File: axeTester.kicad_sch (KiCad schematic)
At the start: 43 parts

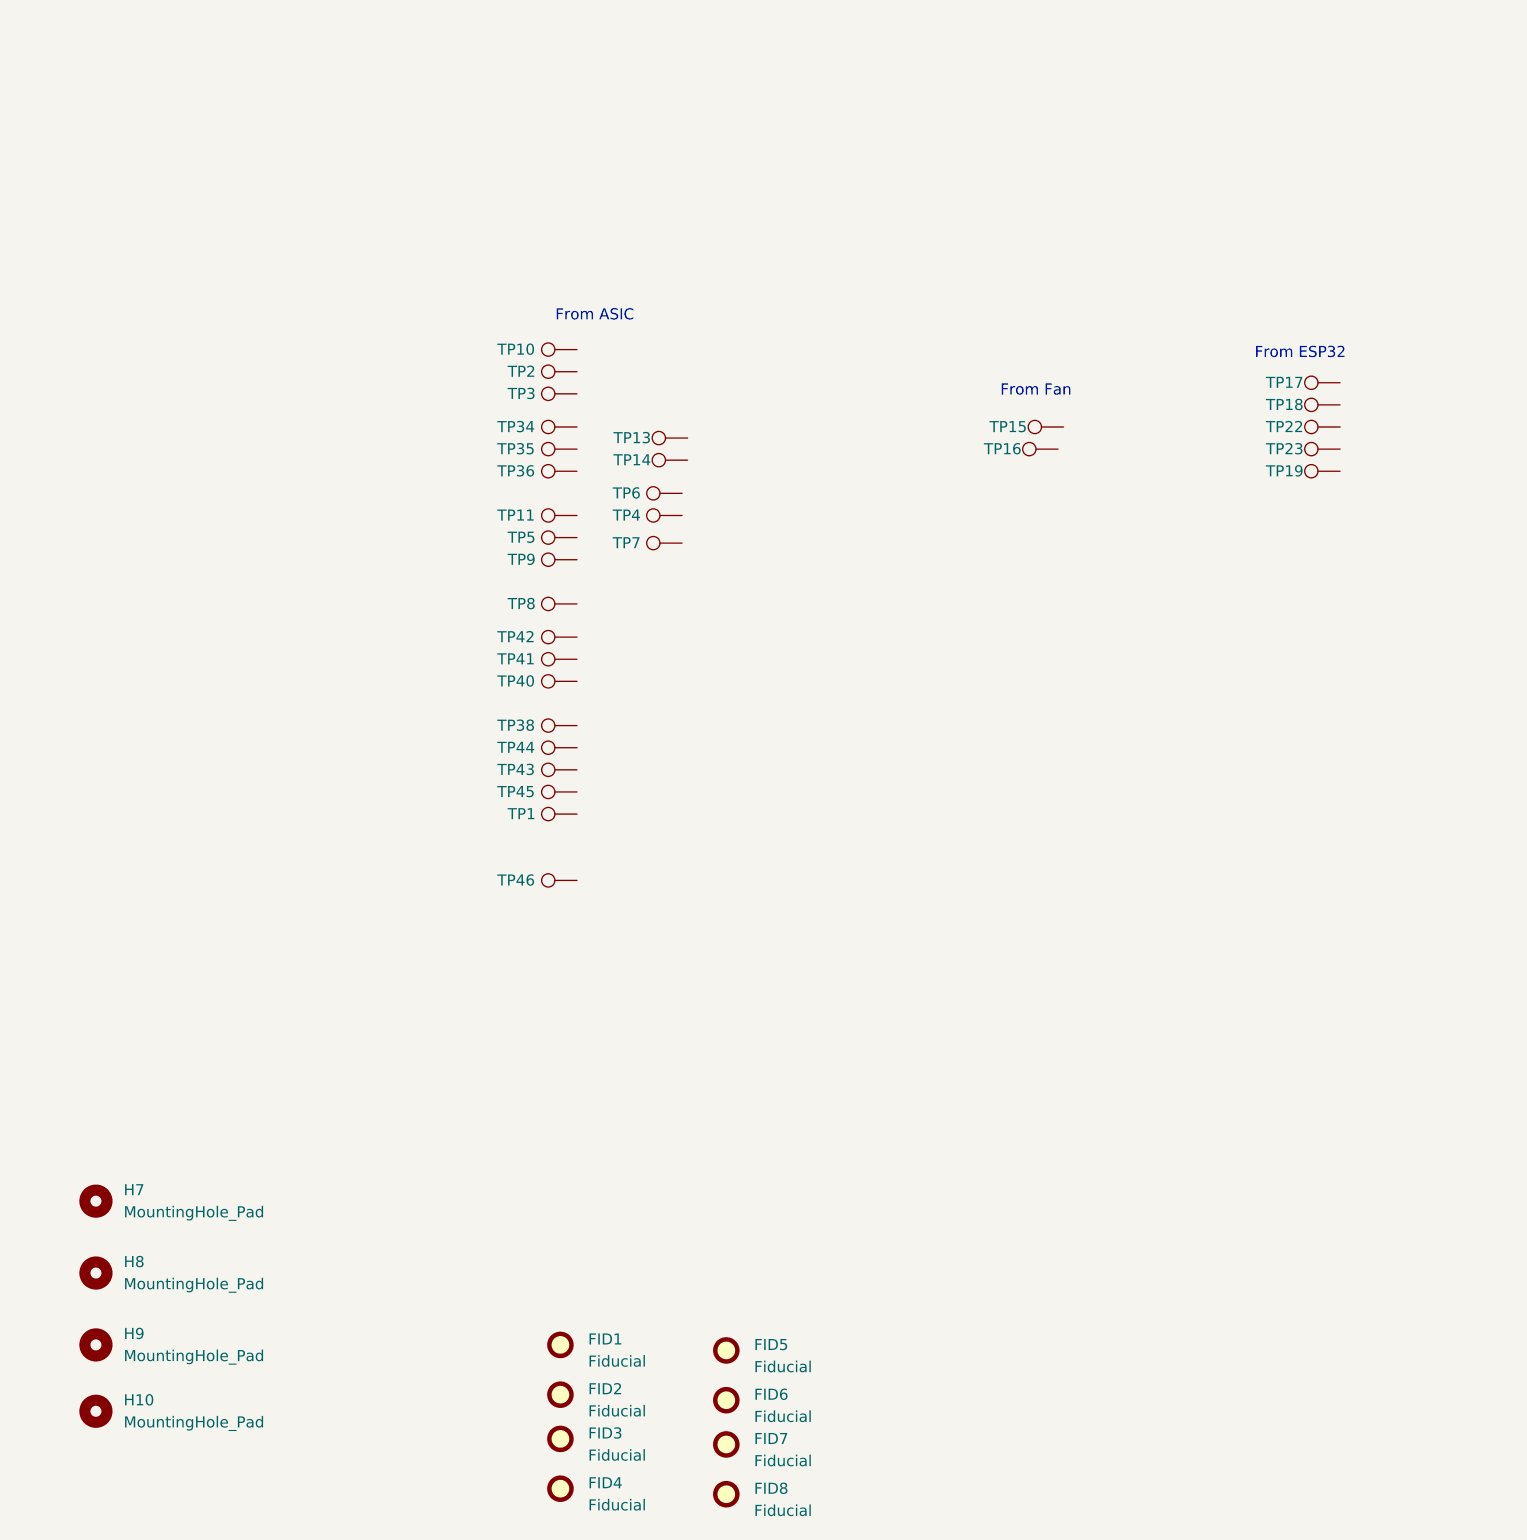
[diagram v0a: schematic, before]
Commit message: switched to more common THT pogo pins. wired up connectors
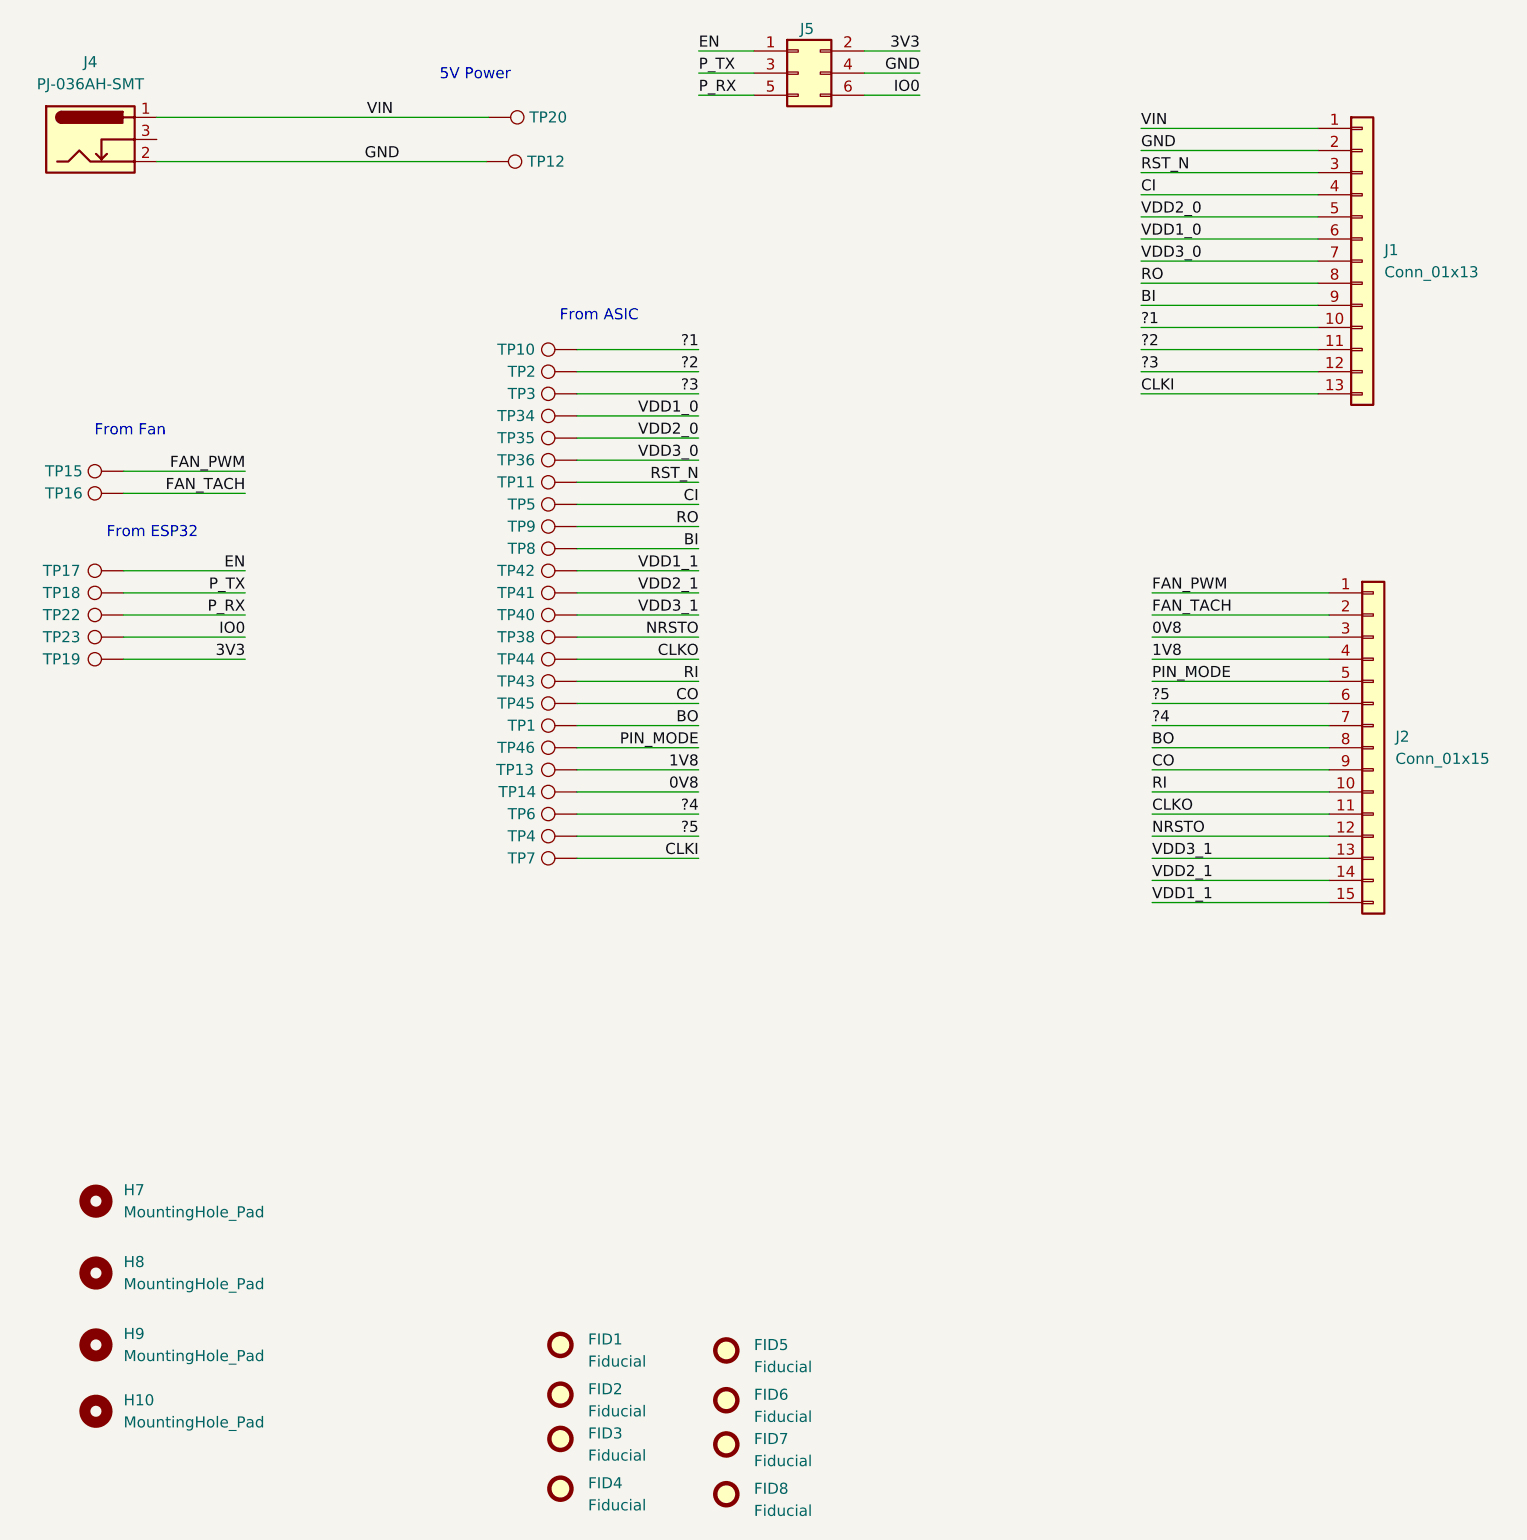
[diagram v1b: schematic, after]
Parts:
- added J1: Conn_01x13, Connector_PinHeader_2.54mm:PinHeader_1x13_P2.54mm_Horizontal, symbol Connector_Generic:Conn_01x13
- added J2: Conn_01x15, Connector_PinHeader_2.54mm:PinHeader_1x15_P2.54mm_Horizontal, symbol Connector_Generic:Conn_01x15
- added J4: PJ-036AH-SMT, Connector_BarrelJack:BarrelJack_CUI_PJ-036AH-SMT_Horizontal, symbol Connector:Barrel_Jack_Switch
- added J5: Conn_02x03_Counter_Clockwise, Connector_PinHeader_2.54mm:PinHeader_2x03_P2.54mm_Vertical, symbol Connector_Generic:Conn_02x03_Odd_Even
- added TP12, TP20: P75-E2, axeTester:pogopin-P75-E2-1.3, symbol Connector:TestPoint
- TP1, TP10, TP11, TP13, TP14, TP15, TP16, TP17, TP18, TP19, TP2, TP22, TP23, TP3, TP34, TP35, TP36, TP38, TP4, TP40, TP41, TP42, TP43, TP44, TP45, TP46, TP5, TP6, TP7, TP8, TP9: value TestPoint -> P50-E2; footprint TestPoint:TestPoint_Pad_D1.5mm -> axeTester:pogopin-P50-E2-0.68
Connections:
- net 1V8: now reaches TP13.1
- net 1V8: now also J2.4 (Pin_4)
- net P_TX: now reaches TP18.1
- net P_TX: now also J5.3 (Pin_3)
- net 3V3: now reaches TP19.1
- net 3V3: now also J5.2 (Pin_2)
- net EN: now reaches TP17.1
- net EN: now also J5.1 (Pin_1)
- net RI: now reaches TP43.1
- net RI: now also J2.10 (Pin_10)
- net CI: now reaches TP5.1
- net CI: now also J1.4 (Pin_4)
- net VDD2_1: now reaches TP41.1
- net VDD2_1: now also J2.14 (Pin_14)
- net BI: now reaches TP8.1
- net BI: now also J1.9 (Pin_9)
- net ?4: now reaches TP6.1
- net ?4: now also J2.7 (Pin_7)
- net VDD1_1: now reaches TP42.1
- net VDD1_1: now also J2.15 (Pin_15)
- net ?5: now reaches TP4.1
- net ?5: now also J2.6 (Pin_6)
- net PIN_MODE: now reaches TP46.1
- net PIN_MODE: now also J2.5 (Pin_5)
- net NRSTO: now reaches TP38.1
- net NRSTO: now also J2.12 (Pin_12)
- net VDD3_1: now reaches TP40.1
- net VDD3_1: now also J2.13 (Pin_13)
- net VDD1_0: now reaches TP34.1
- net VDD1_0: now also J1.6 (Pin_6)
- net FAN_TACH: now reaches TP16.1
- net FAN_TACH: now also J2.2 (Pin_2)
- net CO: now reaches TP45.1
- net CO: now also J2.9 (Pin_9)
- net ?3: now reaches TP3.1
- net ?3: now also J1.12 (Pin_12)
- net 0V8: now reaches TP14.1
- net 0V8: now also J2.3 (Pin_3)
- net FAN_PWM: now reaches TP15.1
- net FAN_PWM: now also J2.1 (Pin_1)
- net P_RX: now reaches TP22.1
- net P_RX: now also J5.5 (Pin_5)
- net RST_N: now reaches TP11.1
- net RST_N: now also J1.3 (Pin_3)
- net ?1: now reaches TP10.1
- net ?1: now also J1.10 (Pin_10)
- net VDD3_0: now reaches TP36.1
- net VDD3_0: now also J1.7 (Pin_7)
- net ?2: now reaches TP2.1
- net ?2: now also J1.11 (Pin_11)
- net IO0: now reaches TP23.1
- net IO0: now also J5.6 (Pin_6)
- net CLKI: now reaches TP7.1
- net CLKI: now also J1.13 (Pin_13)
- net BO: now reaches TP1.1
- net BO: now also J2.8 (Pin_8)
- net VDD2_0: now reaches TP35.1
- net VDD2_0: now also J1.5 (Pin_5)
- net CLKO: now reaches TP44.1
- net CLKO: now also J2.11 (Pin_11)
- net RO: now reaches TP9.1
- net RO: now also J1.8 (Pin_8)
- new net GND: J1.2 (Pin_2), J4.2, J5.4 (Pin_4), TP12.1
- new net VIN: J1.1 (Pin_1), J4.1, TP20.1
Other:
- note added: "5V Power"
- moved on the sheet: TP1, TP11, TP13, TP14, TP15, TP16, TP17, TP18, TP19, TP22, TP23, TP34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
